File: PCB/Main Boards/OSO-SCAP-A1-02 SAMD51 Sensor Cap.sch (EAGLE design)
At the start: 71 parts, among them J1 10118193-0001LF, J2 S2B-PH-SM4-TB(LF)(SN), J3 S3B-PH-SM4-TB(LF)(SN), J4 SM04B-SRSS-TB(LF)(SN), Q1 DMG341, SW1 SPST_TACT-KMR2, SW2 SPST_TACT-KMR2, U1 AP2112-3.3, U2 MCP73831T-2ACI/OT, U3 ATSAMD51G18A-MUT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

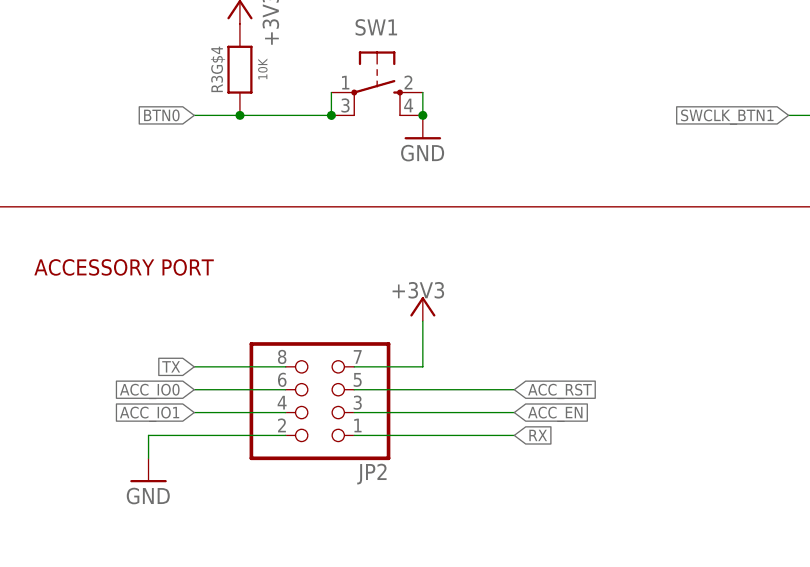
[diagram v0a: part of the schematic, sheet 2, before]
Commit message: rev 2 of sensor cap
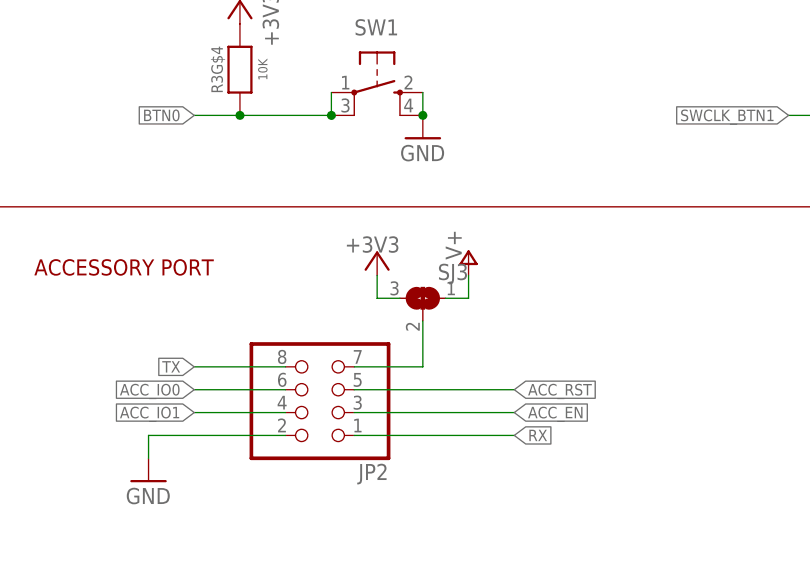
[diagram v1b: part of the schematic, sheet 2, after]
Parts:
- added SJ3: (no value), pygamer-microbuilder:SOLDERJUMPER_2WAY
- C10, C9: device microbuilder:CAP_CERAMIC0805_10MGAP -> microbuilder:CAP_CERAMIC0603_NO
- C11, C12, C13, C15, C16, C3, C6, C7, C8: device microbuilder:CAP_CERAMIC0805-NOOUTLINE -> microbuilder:CAP_CERAMIC0603_NO
- LED: device adafruit:LEDCHIPLED_0805 -> adafruit:LEDCHIPLED_0603
- R10, R4, R5, R6, R7, R8: device microbuilder:RESISTOR0805_NOOUTLINE -> microbuilder:RESISTOR_0603_NOOUT
- R11, R12: value 50K -> 10K; device microbuilder:RESISTOR0805_NOOUTLINE -> microbuilder:RESISTOR_0603_NOOUT
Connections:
- new net ACC_POWER: JP2.7, SJ3.2
- net +3V3: now also SJ3.3; no longer JP2.7
- net V+: now also SJ3.1
